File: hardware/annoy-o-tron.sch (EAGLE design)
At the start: 22 parts, among them J1 USB-MICROB, J2 DM3AT-SF-PEJM5, U1 ATMEGA32-16AU, U2 TPS62203DBVT

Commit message: Replaced ATmega32-16 with ATmega328P. Replace TPS62201 with TPS61201, schematic stil unfinished.
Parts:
- removed L1: 10uH, rcl:R-EU_R0603
- removed U1: ATMEGA32-16AU, annoy-o-library:ATMEGA32-16AU
- removed U2: TPS62203DBVT, annoy-o-library:TPS62203DBVT
- added C11: 1uF, resistor:C-EUC0805K
- added C12: 100nF, resistor:C-EUC0805K
- added C44: 100uF, resistor:CPOL-EU153CLV-0405
- added IC1: TPS61201, texas:TPS61201
- added U3: ATMEGA328P-AU, tudor:ATMEGA328P-AU
- C1: value 4.7uF -> 100nF
- C10, C7: value 100nF -> 10uF; device rcl:C-EUC0805 -> resistor:C-EUC0805K
- C2: value 10uF -> 100nF
- C4: value 100uF -> 100nF; device resistor:CPOL-EU153CLV-0405 -> rcl:C-EUC0805
- C6: device resistor:C-EUC1206K -> resistor:C-EUC0805K
- C8, C9: device rcl:C-EUC0805 -> resistor:C-EUC0805K
- Q1: value (none) -> 8MHz; device special:XTAL/S -> crystal:CRYSTALHC49S
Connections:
- removed net N$7: SP1.2, U1.PD5
- new net N$3: C9.1, IC1.VAUX
- new net RESET: U3.PC6
- new net SPKR: SP1.2, U3.PB1
- new net SS: U3.PB2
- new net VCC/2: C7.2, C8.2, IC1.EN, IC1.UVLO, IC1.VIN
- net BUTTON: now also U3.PD2; no longer U1.PC4
- net D+: now also U3.PC0; no longer U1.PA4
- net D-: now also U3.PC1; no longer U1.PA5
- net GND: now also C1.1, C10.2, C11.2, C12.2, C2.1, C4.1, C44.+, C9.2, IC1.GND, IC1.PGND, IC1.PP, IC1.PP@1, IC1.PP@2, IC1.PS, U3.GND, U3.GND_2, U3.GND_3; no longer C1.2, C10.1, C2.2, C4.+, C9.1, U1.GND, U1.GND_2, U1.GND_3, U1.GND_4, U2.GND
- net MISO: now also U3.PB4; no longer U1.PB6
- net MOSI: now also U3.PB3; no longer U1.PB5
- net N$1: now also IC1.L; no longer L1.1, U2.SW
- net N$2: now also C1.2, U3.AREF; no longer C3.2, U1.AREF
- net N$8: now also C44.-; no longer C4.-
- net RST: no longer U1.~RESET
- net SCK: now also U3.PB5; no longer U1.PB7
- net VCC: now also C10.1, C11.1, C12.1, C2.2, C3.2, C4.2, IC1.FB, IC1.VOUT, U3.AVCC, U3.VCC, U3.VCC_2; no longer C1.1, U2.EN, U2.VI
- net VIN: no longer C10.2, C2.1, C7.2, C8.2, C9.2, L1.2, U1.AVCC, U1.VCC, U1.VCC_2, U1.VCC_3, U2.FB
- net XTAL1: now also Q1.2, U3.PB6; no longer Q1.1, U1.XTAL1
- net XTAL2: now also Q1.1, U3.PB7; no longer Q1.2, U1.XTAL2
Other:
- moved on the sheet: C1, C10, C2, C3, C5, C6, C7, C8, C9, J1, J2, JP1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

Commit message: Finished schematic.
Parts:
- removed C44: 100uF, resistor:CPOL-EU153CLV-0405
- removed J1: USB-MICROB, SparkFun-Connectors:USB-MICROB
- removed S1: (no value), switch-omron:10-XX
- added C13: 100uF, resistor:CPOL-EU153CLV-0405
- added JP3: (no value), pinhead:PINHD-1X2
- added L1: 2.2uH, tudor:SRN3012TA
- added R3: 10k, rcl:R-EU_R0805
- C5: device resistor:C-EUC1206K -> rcl:C-EUC0805K
- JP2: value (none) -> AVR-ISP-6VERT; device pinhead:PINHD-2X3 -> avr-7:AVR-ISP-6VERT
- R1: device resistor:R-EU_R1206W -> rcl:R-EU_R0805
- R2: value 2k2 -> 10k; device resistor:R-EU_R1206W -> rcl:R-EU_R0805
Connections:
- removed net D+: J1.D+, U3.PC0
- removed net D-: J1.D-, R2.1, U3.PC1
- removed net N$8: C44.-, SP1.1
- removed net RST: JP2.5, R1.2
- removed net VIN: J1.VBUS, J2.VCC, JP2.2, R1.1, R2.2
- new net INS: J2.B, R2.2, U3.PB0
- new net N$4: C13.+, SP1.1
- net BUTTON: now also JP3.1, R3.2; no longer S1.S, S1.S1
- net GND: now also C1.2, C13.-, C2.2, C3.2, C4.2, C7.2, C8.2, JP1.1, R2.1, R3.1; no longer C1.1, C2.1, C3.1, C4.1, C44.+, C7.1, C8.1, J1.GND, JP1.2, S1.P, S1.P1
- net N$1: now also L1.1
- net N$2: now also C1.1; no longer C1.2
- net RESET: now also JP2.5, R1.1
- net SS: now also J2.DATA3-CD/CS_N
- net VCC: now also C2.1, C3.1, C4.1, J2.A, J2.VCC, JP2.2, JP3.2, R1.2; no longer C2.2, C3.2, C4.2, JP1.1
- net VCC/2: now also C7.1, C8.1, JP1.2, L1.2; no longer C7.2, C8.2
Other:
- moved on the sheet: C1, C10, C11, C12, C2, C3, C4, C7, C8, C9, IC1, J2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

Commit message: Modifications to schematic. Finished board. Added part list and hardware README.
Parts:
- removed SP1: AL11P, buzzer:AL11P
- added JP4: (no value), pinhead:PINHD-1X2
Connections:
- net INS: now also J2.A, U3.PB1; no longer J2.B, U3.PB0
- net N$4: now also JP4.1; no longer SP1.1
- net SPKR: now also JP4.2, U3.PB0; no longer SP1.2, U3.PB1
- net VCC: now also J2.B; no longer J2.A
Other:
- moved on the sheet: C13
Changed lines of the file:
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@@
 </classes>
 <parts>
-<part name="SP1" library="buzzer" deviceset="AL11P" device=""/>
 <part name="GND5" library="supply1" deviceset="GND" device=""/>
 <part name="R1" library="rcl" deviceset="R-EU_" device="R0805" value="10k"/>
@@
 <part name="GND7" library="supply1" deviceset="GND" device=""/>
 <part name="JP3" library="pinhead" deviceset="PINHD-1X2" device=""/>
+<part name="JP4" library="pinhead" deviceset="PINHD-1X2" device=""/>
 </parts>
 <sheets>
@@
 </plain>
 <instances>
-<instance part="SP1" gate="G$1" x="370.84" y="467.36"/>
-<instance part="GND5" gate="1" x="358.14" y="441.96"/>
+<instance part="GND5" gate="1" x="386.08" y="439.42"/>
 <instance part="R1" gate="G$1" x="180.34" y="114.3" rot="R90"/>
 <instance part="Q1" gate="G$1" x="408.94" y="99.06" rot="R90"/>
@@
 <instance part="C6" gate="G$1" x="396.24" y="109.22" rot="R90"/>
 <instance part="GND6" gate="1" x="386.08" y="78.74"/>
-<instance part="C13" gate="G$1" x="358.14" y="457.2" rot="MR0"/>
+<instance part="C13" gate="G$1" x="386.08" y="454.66" rot="MR0"/>
 <instance part="JP1" gate="G$1" x="45.72" y="292.1" rot="R180"/>
 <instance part="J2" gate="G$1" x="109.22" y="454.66"/>
@@
 <instance part="GND7" gate="1" x="431.8" y="436.88"/>
 <instance part="JP3" gate="G$1" x="416.56" y="467.36" rot="R180"/>
+<instance part="JP4" gate="G$1" x="370.84" y="467.36" rot="R180"/>
 </instances>
 <busses>
@@
 </segment>
 <segment>
-<pinref part="J2" gate="G$1" pin="A"/>
-<wire x1="124.46" y1="439.42" x2="132.08" y2="439.42" width="0.1524" layer="91"/>
-<label x="132.08" y="439.42" size="1.778" layer="95" font="vector"/>
+<pinref part="J2" gate="G$1" pin="B"/>
+<wire x1="124.46" y1="436.88" x2="132.08" y2="436.88" width="0.1524" layer="91"/>
+<label x="132.08" y="436.88" size="1.778" layer="95" font="vector"/>
 </segment>
 </net>
@@
 <segment>
 <pinref part="GND5" gate="1" pin="GND"/>
-<wire x1="358.14" y1="444.5" x2="358.14" y2="452.12" width="0.1524" layer="91"/>
+<wire x1="386.08" y1="441.96" x2="386.08" y2="449.58" width="0.1524" layer="91"/>
 <pinref part="C13" gate="G$1" pin="-"/>
 </segment>
@@
 <net name="SPKR" class="0">
 <segment>
-<pinref part="SP1" gate="G$1" pin="2"/>
-<wire x1="383.54" y1="467.36" x2="375.92" y2="467.36" width="0.1524" layer="91"/>
-<label x="383.54" y="467.36" size="1.778" layer="95"/>
-</segment>
-<segment>
-<pinref part="U3" gate="A" pin="PB1"/>
-<wire x1="137.16" y1="91.44" x2="129.54" y2="91.44" width="0.1524" layer="91"/>
-<label x="129.54" y="91.44" size="1.778" layer="95" font="vector" rot="R180"/>
+<label x="386.08" y="467.36" size="1.778" layer="95"/>
+<pinref part="JP4" gate="G$1" pin="2"/>
+<wire x1="386.08" y1="467.36" x2="373.38" y2="467.36" width="0.1524" layer="91"/>
+</segment>
+<segment>
+<pinref part="U3" gate="A" pin="PB0"/>
+<wire x1="137.16" y1="93.98" x2="129.54" y2="93.98" width="0.1524" layer="91"/>
+<label x="129.54" y="93.98" size="1.778" layer="95" font="vector" rot="R180"/>
 </segment>
 </net>
@@
 <net name="INS" class="0">
 <segment>
-<pinref part="J2" gate="G$1" pin="B"/>
-<wire x1="124.46" y1="436.88" x2="132.08" y2="436.88" width="0.1524" layer="91"/>
-<label x="132.08" y="436.88" size="1.778" layer="95" font="vector"/>
-</segment>
-<segment>
 <pinref part="R2" gate="G$1" pin="2"/>
 <wire x1="160.02" y1="454.66" x2="160.02" y2="462.28" width="0.1524" layer="91"/>
@@
 </segment>
 <segment>
-<pinref part="U3" gate="A" pin="PB0"/>
-<wire x1="137.16" y1="93.98" x2="129.54" y2="93.98" width="0.1524" layer="91"/>
-<label x="129.54" y="93.98" size="1.778" layer="95" font="vector" rot="R180"/>
+<pinref part="J2" gate="G$1" pin="A"/>
+<wire x1="124.46" y1="439.42" x2="132.08" y2="439.42" width="0.1524" layer="91"/>
+<label x="132.08" y="439.42" size="1.778" layer="95" font="vector"/>
+</segment>
+<segment>
+<pinref part="U3" gate="A" pin="PB1"/>
+<wire x1="137.16" y1="91.44" x2="129.54" y2="91.44" width="0.1524" layer="91"/>
+<label x="129.54" y="91.44" size="1.778" layer="95" font="vector" rot="R180"/>
 </segment>
 </net>
@@
 <segment>
 <pinref part="C13" gate="G$1" pin="+"/>
-<pinref part="SP1" gate="G$1" pin="1"/>
-<wire x1="358.14" y1="459.74" x2="358.14" y2="467.36" width="0.1524" layer="91"/>
-<wire x1="358.14" y1="467.36" x2="365.76" y2="467.36" width="0.1524" layer="91"/>
-</segment>
-</net>
+<pinref part="JP4" gate="G$1" pin="1"/>
+<wire x1="386.08" y1="457.2" x2="386.08" y2="464.82" width="0.1524" layer="91"/>
+<wire x1="386.08" y1="464.82" x2="373.38" y2="464.82" width="0.1524" layer="91"/>
+</segment>
+</net>

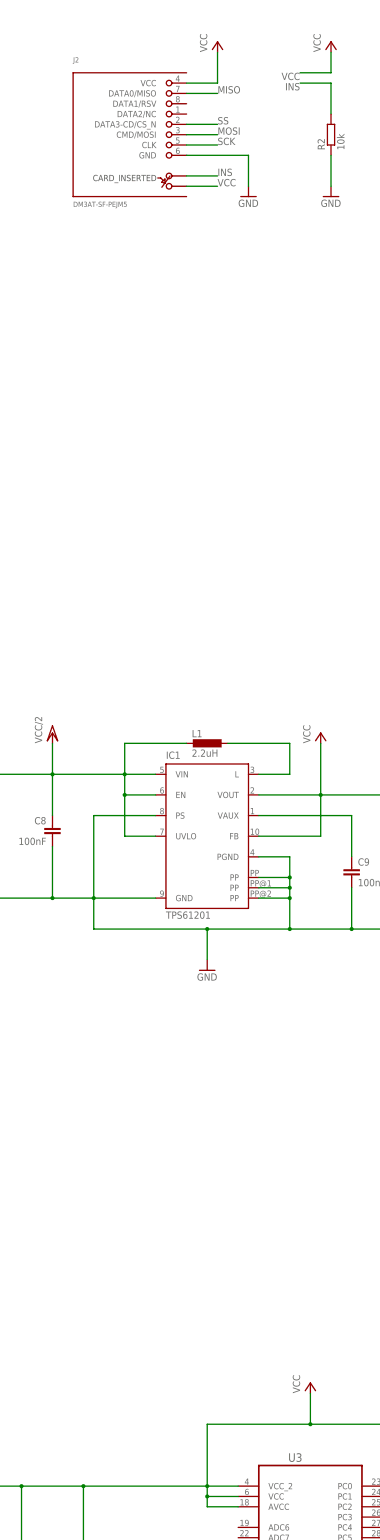
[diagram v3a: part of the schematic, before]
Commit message: Made capacitor packages uniform. Naming changes in schematic. Board corrections for new packages.
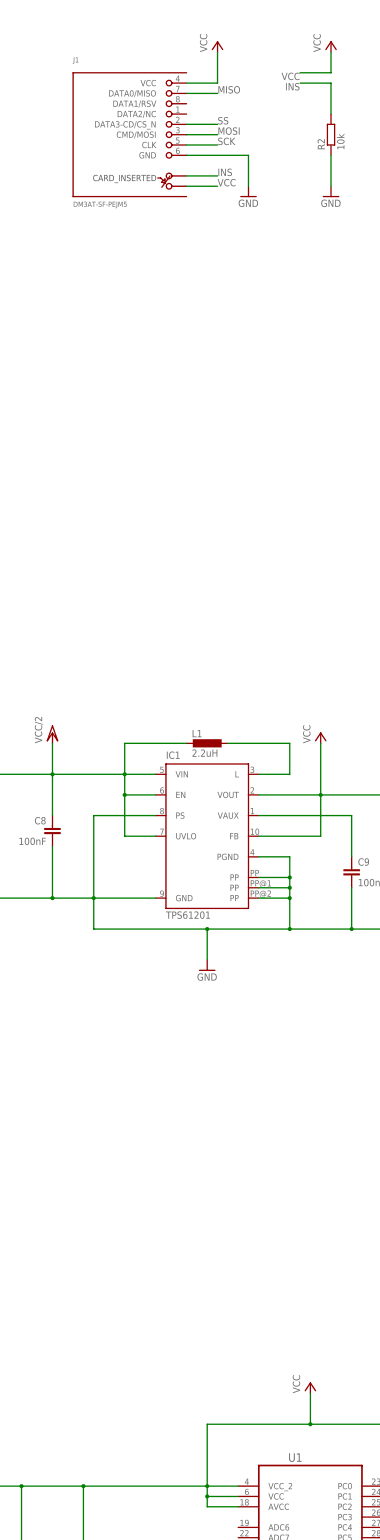
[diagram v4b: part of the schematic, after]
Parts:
- C1, C2, C3, C4: device rcl:C-EUC0805 -> rcl:C-EUC0805K
- C10, C11, C12, C6, C7, C8, C9: device resistor:C-EUC0805K -> rcl:C-EUC0805K
- C13: device resistor:CPOL-EU153CLV-0405 -> rcl:CPOL-EU153CLV-0405
- renumbered J2 to J1, U3 to U1
